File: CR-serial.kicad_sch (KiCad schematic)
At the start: 32 parts, among them J1 USB, J2 GPIO, J3 UART0, J4 UART1, J5 UART2, J6 UART3_HV, J7 RS232_0, J8 RS232_1, U1 CP2108-xxx-xM, U2 MAX232

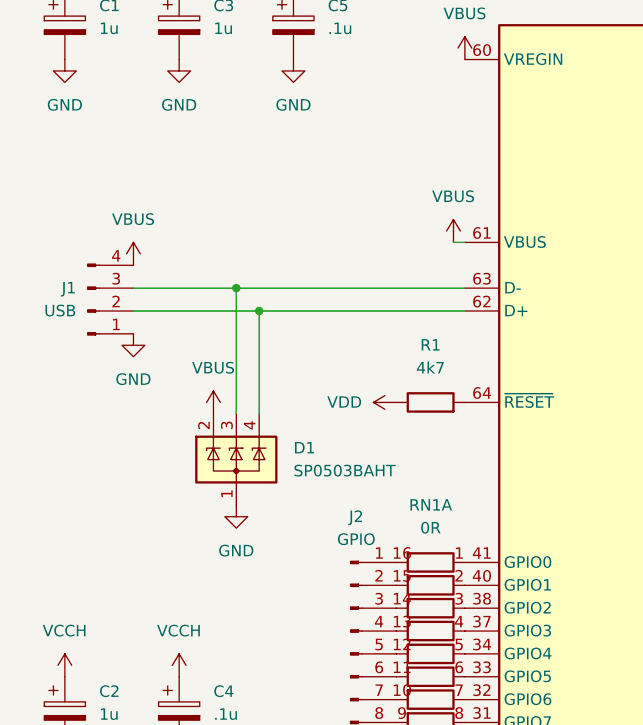
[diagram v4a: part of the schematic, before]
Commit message: Change USB connector to USB-B
`--patience` is recommended
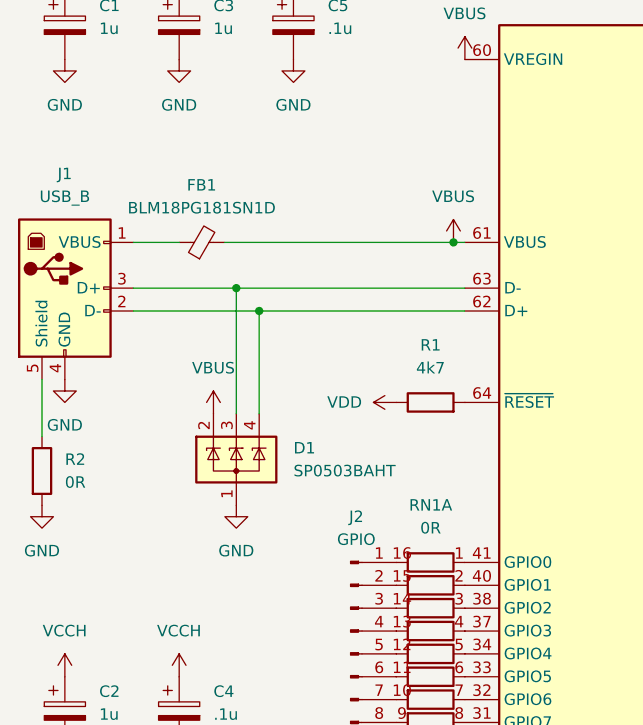
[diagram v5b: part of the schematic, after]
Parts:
- removed J1: USB, Connector_PinHeader_2.54mm:PinHeader_1x04_P2.54mm_Vertical, symbol Connector:Conn_01x04_Pin
- added FB1: BLM18PG181SN1D, Inductor_SMD:L_0201_0603Metric, symbol Device:FerriteBead_Small
- added J1: USB_B, Connector_USB:USB_B_OST_USB-B1HSxx_Horizontal, symbol Connector:USB_B
- added R2: 0R, Resistor_SMD:R_0603_1608Metric, symbol Device:R
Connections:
- net GND: now also J1.4 (GND), R2.2
- net VBUS: now also FB1.2
- net at D1.4 (K), U1.62 (D+): now also J1.2 (D-)
- net at D1.3 (K), U1.63 (D-): now also J1.3 (D+)
- new net: FB1.1, J1.1 (VBUS)
- new net: J1.5 (Shield), R2.1

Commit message: Change passives to 0603 size
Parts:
- C1, C2, C3, C4, C5, C6, C7, C8, C9: footprint Capacitor_SMD:C_1206_3216Metric -> Capacitor_SMD:C_0603_1608Metric
- R1: footprint Resistor_SMD:R_0805_2012Metric -> Resistor_SMD:R_0603_1608Metric
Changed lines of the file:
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@@
 			)
 		)
-		(property "Footprint" "Capacitor_SMD:C_1206_3216Metric"
+		(property "Footprint" "Capacitor_SMD:C_0603_1608Metric"
 			(at 197.8152 68.58 0)
 			(effects
@@
 			)
 		)
-		(property "Footprint" "Capacitor_SMD:C_1206_3216Metric"
+		(property "Footprint" "Capacitor_SMD:C_0603_1608Metric"
 			(at 257.81 82.2452 0)
 			(effects
@@
 			)
 		)
-		(property "Footprint" "Capacitor_SMD:C_1206_3216Metric"
+		(property "Footprint" "Capacitor_SMD:C_0603_1608Metric"
 			(at 41.6052 120.65 0)
 			(effects
@@
 			)
 		)
-		(property "Footprint" "Capacitor_SMD:C_1206_3216Metric"
+		(property "Footprint" "Capacitor_SMD:C_0603_1608Metric"
 			(at 248.6152 68.58 0)
 			(effects
@@
 			)
 		)
-		(property "Footprint" "Resistor_SMD:R_0805_2012Metric"
+		(property "Footprint" "Resistor_SMD:R_0603_1608Metric"
 			(at 68.58 84.328 90)
 			(effects
@@
 			)
 		)
-		(property "Footprint" "Capacitor_SMD:C_1206_3216Metric"
+		(property "Footprint" "Capacitor_SMD:C_0603_1608Metric"
 			(at 28.9052 44.45 0)
 			(effects
@@
 			)
 		)
-		(property "Footprint" "Capacitor_SMD:C_1206_3216Metric"
+		(property "Footprint" "Capacitor_SMD:C_0603_1608Metric"
 			(at 28.9052 120.65 0)
 			(effects
@@
 			)
 		)
-		(property "Footprint" "Capacitor_SMD:C_1206_3216Metric"
+		(property "Footprint" "Capacitor_SMD:C_0603_1608Metric"
 			(at 41.6052 44.45 0)
 			(effects
@@
 			)
 		)
-		(property "Footprint" "Capacitor_SMD:C_1206_3216Metric"
+		(property "Footprint" "Capacitor_SMD:C_0603_1608Metric"
 			(at 54.3052 44.45 0)
 			(effects
@@
 			)
 		)
-		(property "Footprint" "Capacitor_SMD:C_1206_3216Metric"
+		(property "Footprint" "Capacitor_SMD:C_0603_1608Metric"
 			(at 255.27 72.6948 0)
 			(effects

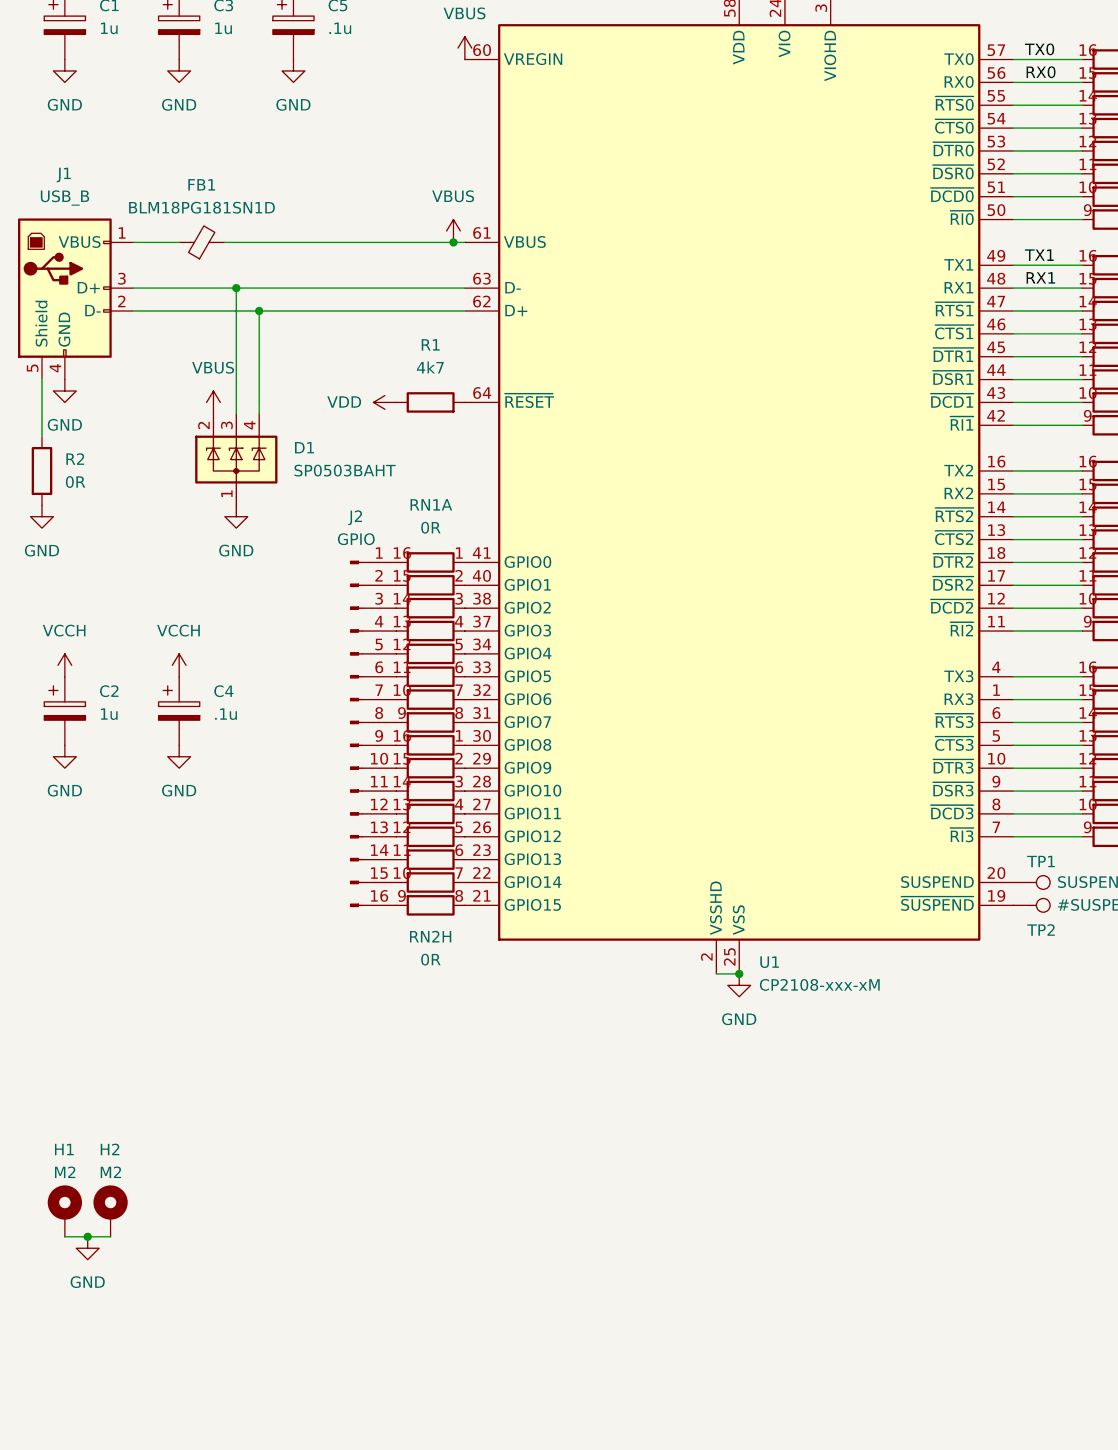
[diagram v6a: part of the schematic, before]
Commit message: Change USB protection: add ECMF02-4CMX8
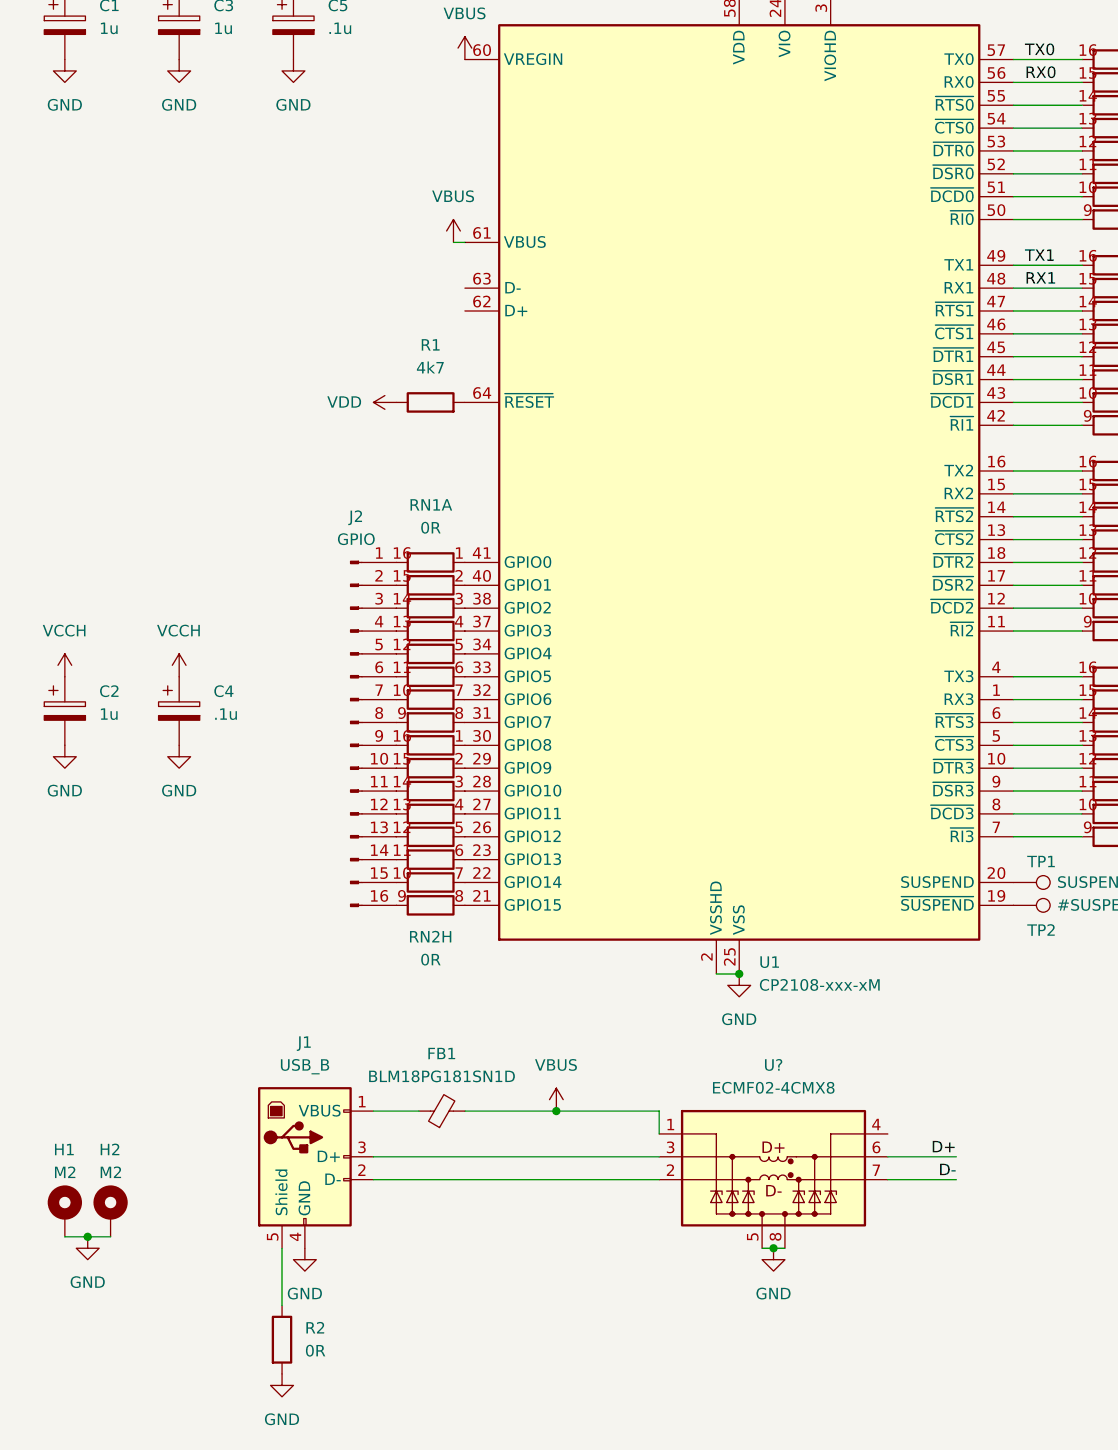
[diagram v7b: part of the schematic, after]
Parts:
- removed D1: SP0503BAHT, Package_TO_SOT_SMD:SOT-143, symbol Power_Protection:SP0503BAHT
- added U?: ECMF02-4CMX8, QCP_parts:ST_UQFN-8L_1.15x2.45mm_P0.5mm, symbol QCP_parts:ECMF02-4CMX8
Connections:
- net GND: now also U?.5 (GND), U?.8 (GND)
- net VBUS: now also U?.1 (VBUS)
- net at U1.62 (D+): no longer J1.2 (D-)
- net at U1.63 (D-): no longer J1.3 (D+)
- new net: J1.2 (D-), U?.2 (D-_in)
- new net: J1.3 (D+), U?.3 (D+_in)
- new net D+: U?.6 (D+_out)
- new net D-: U?.7 (D-_out)
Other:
- moved on the sheet: FB1, J1, R2
